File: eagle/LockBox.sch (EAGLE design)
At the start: 16 parts

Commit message: First draft of LockBox.sch is complete and ready for review
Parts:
- added D1: 1N4004, LockBox:1N4004
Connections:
- new net N$1: D1.A, JP1.2, U$4.C
- net +12V: now also D1.C
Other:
- note added: "G06 - Practicum"
- note added: "Solonoid Driver"
- moved on the sheet: JP1, R4
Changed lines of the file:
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@@
 <setting verticaltext="up"/>
 </settings>
-<grid distance="0.025" unitdist="inch" unit="inch" style="lines" multiple="1" display="yes" altdistance="0.01" altunitdist="inch" altunit="inch"/>
+<grid distance="0.1" unitdist="inch" unit="inch" style="lines" multiple="1" display="yes" altdistance="0.01" altunitdist="inch" altunit="inch"/>
 <layers>
 <layer number="1" name="Top" color="4" fill="1" visible="no" active="no"/>
@@
 <part name="SUPPLY1" library="supply2" deviceset="+12V" device=""/>
 <part name="SUPPLY2" library="supply2" deviceset="+12V" device=""/>
+<part name="D1" library="LockBox" deviceset="1N4004" device=""/>
 </parts>
 <sheets>
@@
 <wire x1="78.74" y1="2.54" x2="78.74" y2="49.53" width="0.635" layer="97"/>
 <text x="15.24" y="43.18" size="3.81" layer="97">Interface - NES Controller</text>
+<wire x1="147.32" y1="100.965" x2="220.98" y2="100.965" width="0.635" layer="97"/>
+<wire x1="147.32" y1="100.965" x2="147.32" y2="38.735" width="0.635" layer="97"/>
+<wire x1="147.32" y1="38.735" x2="220.98" y2="38.735" width="0.635" layer="97"/>
+<wire x1="220.98" y1="38.735" x2="220.98" y2="100.965" width="0.635" layer="97"/>
+<text x="167.64" y="95.25" size="3.81" layer="97">Solonoid Driver</text>
+<text x="162.56" y="25.4" size="6.4516" layer="97">G06 - Practicum</text>
 </plain>
 <instances>
@@
 <instance part="U$5" gate="G$1" x="199.39" y="135.89"/>
 <instance part="R3" gate="G$1" x="166.37" y="157.48" rot="R90"/>
-<instance part="U$4" gate="GATE" x="173.99" y="71.12"/>
+<instance part="U$4" gate="GATE" x="167.005" y="64.77"/>
 <instance part="U$6" gate="G$1" x="26.67" y="20.32" smashed="yes" rot="MR0">
 <attribute name="NAME" x="19.05" y="22.86" size="1.778" layer="95" rot="MR0"/>
@@
 </instance>
 <instance part="C2" gate="G$1" x="74.93" y="147.32"/>
-<instance part="R4" gate="G$1" x="162.56" y="71.12"/>
-<instance part="GND6" gate="1" x="194.31" y="50.8"/>
-<instance part="JP1" gate="G$1" x="206.375" y="92.075"/>
+<instance part="R4" gate="G$1" x="155.575" y="64.77"/>
+<instance part="GND6" gate="1" x="187.325" y="44.45"/>
+<instance part="JP1" gate="G$1" x="213.995" y="80.645"/>
 <instance part="SUPPLY1" gate="+12V" x="40.64" y="159.385"/>
-<instance part="SUPPLY2" gate="+12V" x="179.705" y="97.155"/>
+<instance part="SUPPLY2" gate="+12V" x="172.72" y="85.725"/>
+<instance part="D1" gate="1" x="187.325" y="79.375" smashed="yes" rot="R90">
+<attribute name="NAME" x="179.705" y="79.8576" size="1.778" layer="95"/>
+<attribute name="VALUE" x="176.53" y="77.0636" size="1.778" layer="96"/>
+</instance>
 </instances>
 <busses>
@@
 <segment>
 <pinref part="U$4" gate="GATE" pin="E"/>
-<wire x1="194.31" y1="58.42" x2="194.31" y2="53.34" width="0.1524" layer="91"/>
+<wire x1="187.325" y1="52.07" x2="187.325" y2="46.99" width="0.1524" layer="91"/>
 <pinref part="GND6" gate="1" pin="GND"/>
 </segment>
@@
 <label x="93.98" y="71.12" size="1.778" layer="95"/>
 <pinref part="R4" gate="G$1" pin="2"/>
-<wire x1="173.99" y1="71.12" x2="167.64" y2="71.12" width="0.1524" layer="91"/>
+<wire x1="167.005" y1="64.77" x2="160.655" y2="64.77" width="0.1524" layer="91"/>
 </segment>
 <segment>
 <pinref part="R4" gate="G$1" pin="1"/>
 <pinref part="U$1" gate="G$1" pin="PD5"/>
-<wire x1="157.48" y1="71.12" x2="81.28" y2="71.12" width="0.1524" layer="91"/>
+<wire x1="150.495" y1="64.77" x2="139.7" y2="64.77" width="0.1524" layer="91"/>
+<wire x1="139.7" y1="64.77" x2="139.7" y2="71.12" width="0.1524" layer="91"/>
+<wire x1="139.7" y1="71.12" x2="81.28" y2="71.12" width="0.1524" layer="91"/>
 </segment>
 </net>
@@
 <pinref part="SUPPLY2" gate="+12V" pin="+12V"/>
 <pinref part="JP1" gate="G$1" pin="1"/>
-<wire x1="179.705" y1="94.615" x2="203.835" y2="94.615" width="0.1524" layer="91"/>
-</segment>
-</net>
+<wire x1="172.72" y1="83.185" x2="187.325" y2="83.185" width="0.1524" layer="91"/>
+<pinref part="D1" gate="1" pin="C"/>
+<wire x1="187.325" y1="83.185" x2="211.455" y2="83.185" width="0.1524" layer="91"/>
+<wire x1="187.325" y1="81.915" x2="187.325" y2="83.185" width="0.1524" layer="91"/>
+<junction x="187.325" y="83.185"/>
+</segment>
+</net>
+<net name="N$1" class="0">
+<segment>
+<pinref part="JP1" gate="G$1" pin="2"/>
+<wire x1="211.455" y1="80.645" x2="194.945" y2="80.645" width="0.1524" layer="91"/>
+<wire x1="194.945" y1="80.645" x2="194.945" y2="75.565" width="0.1524" layer="91"/>
+<wire x1="194.945" y1="75.565" x2="187.325" y2="75.565" width="0.1524" layer="91"/>
+<pinref part="D1" gate="1" pin="A"/>
+<wire x1="187.325" y1="75.565" x2="187.325" y2="76.835" width="0.1524" layer="91"/>
+<wire x1="187.325" y1="75.565" x2="187.325" y2="72.39" width="0.1524" layer="91"/>
+<junction x="187.325" y="75.565"/>
+<pinref part="U$4" gate="GATE" pin="C"/>
+</segment>
+</net>

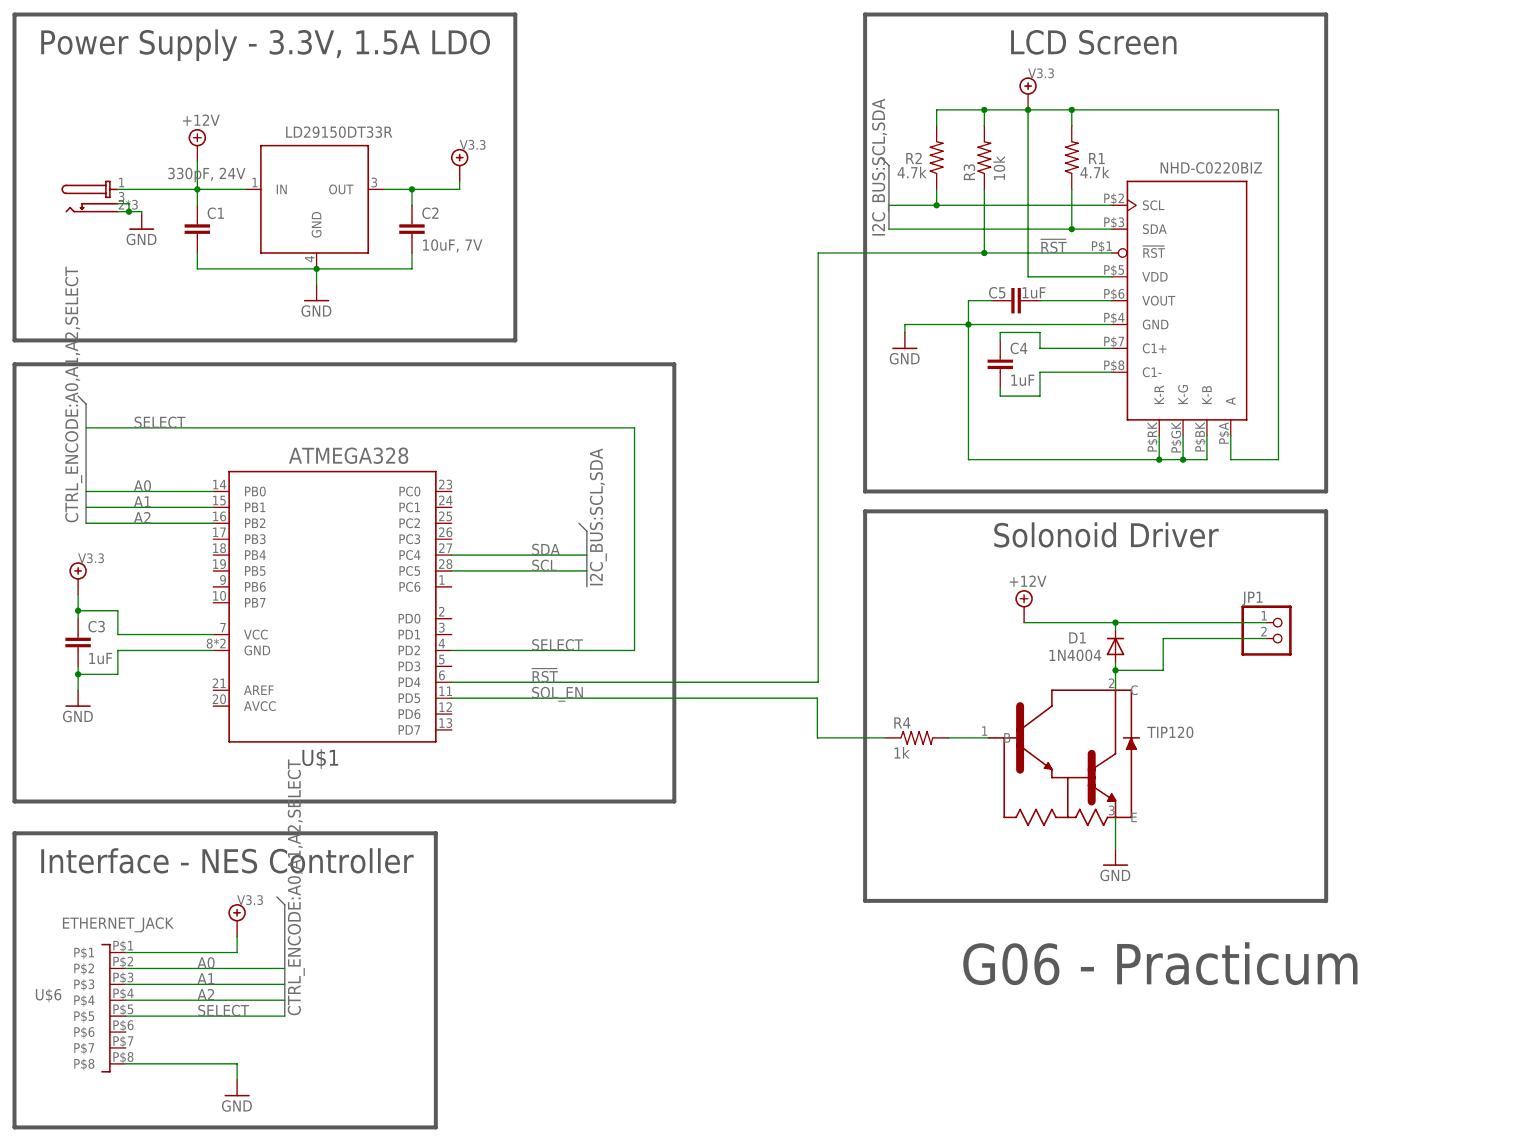
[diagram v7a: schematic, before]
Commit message: Added bus and related nets for LED color control on the LCD screen
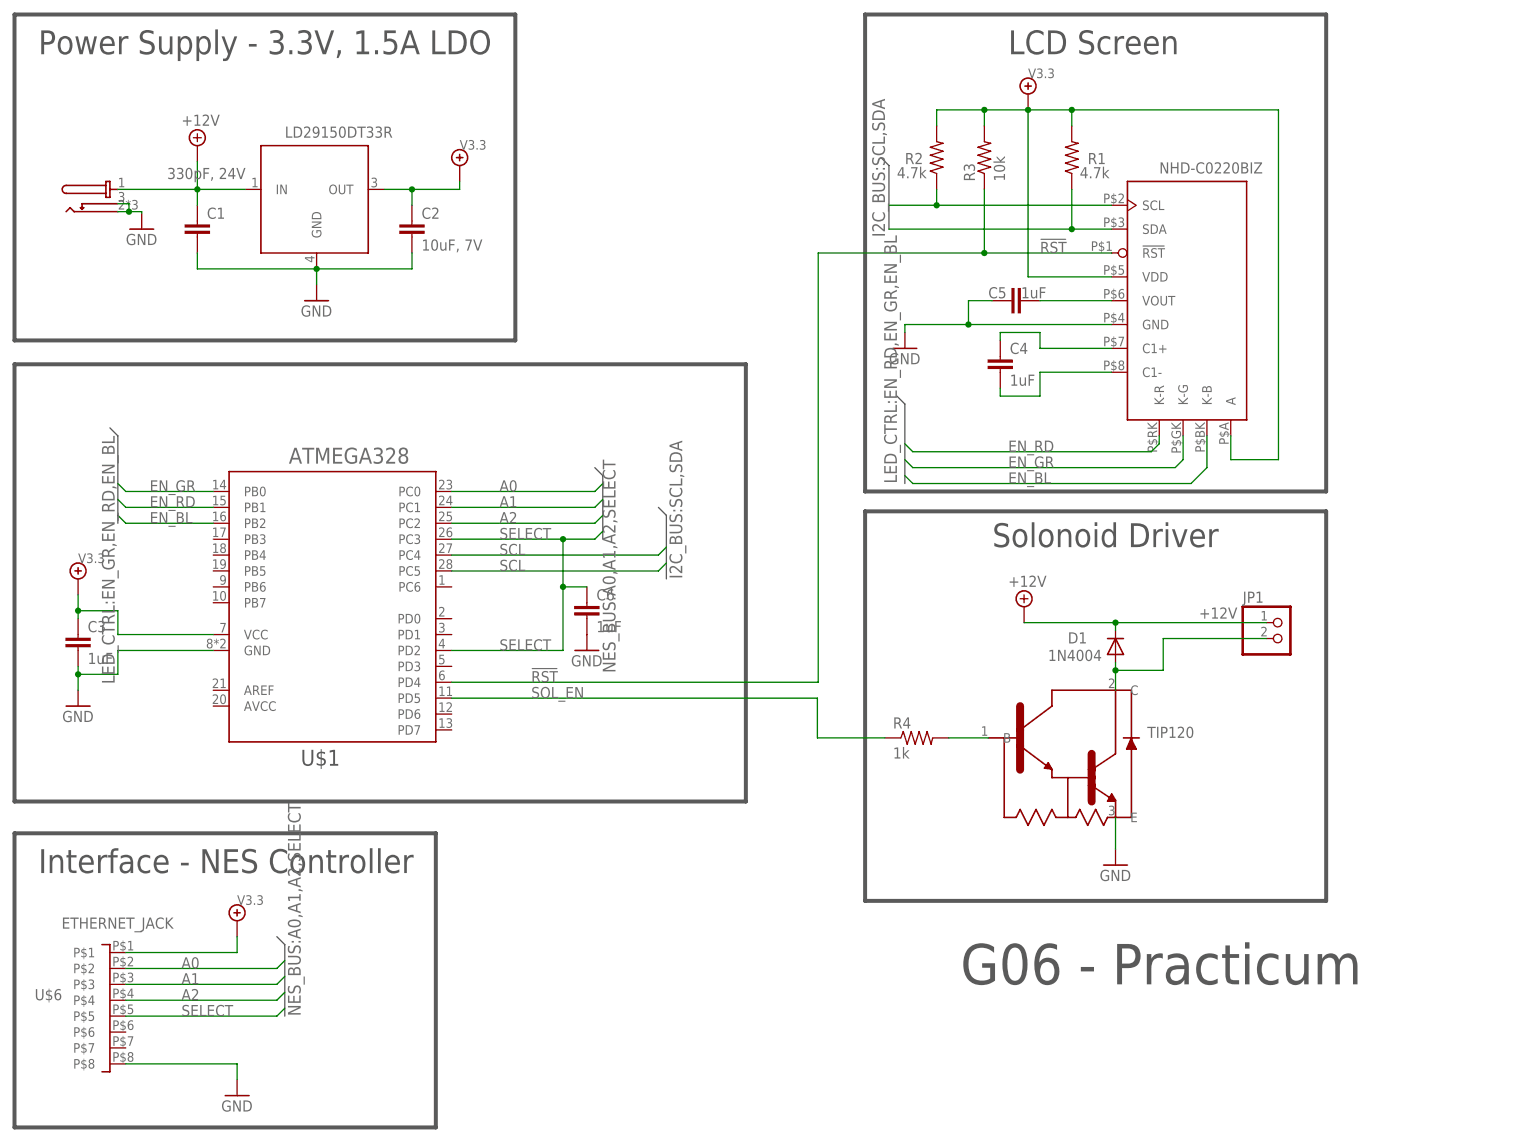
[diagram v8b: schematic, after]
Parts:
- added C6: 1uF, LockBox:C
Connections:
- new net EN_BL: U$1.PB2, U$5.K-B
- new net EN_GR: U$1.PB0, U$5.K-G
- new net EN_RD: U$1.PB1, U$5.K-R
- net A0: now also U$1.PC0; no longer U$1.PB0
- net A1: now also U$1.PC1; no longer U$1.PB1
- net A2: now also U$1.PC2; no longer U$1.PB2
- net GND: now also C6.2; no longer U$5.K-B, U$5.K-G, U$5.K-R
- net SCL: now also U$1.PC4
- net SDA: no longer U$1.PC4
- net SELECT: now also C6.1, U$1.PC3
